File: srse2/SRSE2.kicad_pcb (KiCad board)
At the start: 2 copper layers, 82 x 72 mm, 93 parts, among them J1 s88-N, J2 CAN, P1 I2S, P10 PIC_SPARE, P11 RS485 TERM, P12 RS485, P13 CONN_01X03, P15 S88I, P17 RA5, P18 CONN_01X03, P19 CONN_01X02, P2 CONN_01X09, P20 O2P-Rst, P3 CONN_01X02, P4 CONN_01X04, P5 CONN_01X04, P6 ISO_I2C, P7 CAN_TERM, P8 CAN, P9 PIC_I2C, U1 Omega2, U10 OKI-78SR, U2 ADuM1250, U3 SN65HVD230, U4 PIC18F25K80, U5 HR911105A, U6 MAX485, U7 TPS5430DDA, U8 CD4504, U9 LM317, Y1 16MHz

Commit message: new SRSEII JLCPCB production files Version 1.8
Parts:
- U2, U6: footprint w_smd_dil:so-8 -> Package_SO:SOIC-8_3.9x4.9mm_P1.27mm
- U8: footprint w_smd_dil:so-16 -> Package_SO:SO-16_3.9x9.9mm_P1.27mm
- moved R25 5.72 mm to (122.0, 118.2)
- moved R24 3.64 mm to (126.5, 118.2), turned to 0 degrees
- moved G*** 1.65 mm to (150.8, 76.2)
- moved D3 0.56 mm to (125.2, 87.6)
- moved U10 0.50 mm to (117.7, 79.6)
- moved U9 0.41 mm to (105.7, 121.3)
- moved P13 0.35 mm to (113.2, 82.2)
- moved R9 0.29 mm to (166.4, 100.2)
- moved D2 0.26 mm to (125.2, 92.4)
- moved C1 0.14 mm to (143.6, 113.0)
- moved P4 0.11 mm to (171.4, 118.1)
- moved P20 0.11 mm to (166.0, 120.2)
- moved R104 0.08 mm to (113.1, 87.6)
- turned R103 to -90 degrees
- turned U2 to 0 degrees
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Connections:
- net Net-(D100-Pad1) renamed /PH
- net Net-(L100-Pad2) renamed /Vout
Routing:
- net +5V: track 107.5 -> 178.9 mm, vias 8 -> 10
- net VCC: track 250.1 -> 303.1 mm, vias 3 -> 4
- net /12V: track 7.40 -> 51.1 mm, vias 0 -> 1
- net +24V: track 55.3 -> 84.5 mm, vias 0 -> 2
- net GND: track 181.3 -> 200.1 mm, vias 34 -> 57
- net /Vout: track 0.00 -> 18.5 mm
- net Net-(P12-Pad4): track 10.5 -> 27.2 mm, vias 0 -> 2
- net Net-(D3-Pad1): track 0.00 -> 13.9 mm
- net Net-(R26-Pad1): track 0.00 -> 13.9 mm
- net /S88_DATA: track 5.58 -> 18.3 mm
- net /Vdd: track 10.0 -> 22.1 mm, vias 0 -> 1
- net Net-(R101-Pad2): track 0.00 -> 12.1 mm
- net Net-(P11-Pad2): track 8.05 -> 19.9 mm
- net Net-(D2-Pad1): track 0.00 -> 11.1 mm
- net Net-(C100-Pad2): track 0.00 -> 10.8 mm
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- added copper zone on F.Cu, net /PH
- added copper zone on F.Cu, net /Vout

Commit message: add new production ZIP
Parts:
- added REF**: Inlay, SRSE2:Inlay, F.Cu at (140.8, 109.8)
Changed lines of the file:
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@@
+    )
+  )
+  (footprint "SRSE2:Inlay" (layer "F.Cu")
+    (at 140.85 109.85)
+    (attr smd)
+    (fp_text reference "REF**" (at 0 -0.5 unlocked) (layer "F.SilkS")
+      (effects (font (size 1 1) (thickness 0.15)))
+    )
+    (fp_text value "Inlay" (at 0 1 unlocked) (layer "F.Fab")
+      (effects (font (size 1 1) (thickness 0.15)))
+    )
+    (fp_text user "${REFERENCE}" (at 0 2.5 unlocked) (layer "F.Fab")
+      (effects (font (size 1 1) (thickness 0.15)))
+    )
+    (fp_circle (center -33 20) (end -28 20) (layer "F.SilkS") (width 0.12) (fill none))
+    (fp_circle (center 33 -20) (end 38.211644 -20) (layer "F.SilkS") (width 0.12) (fill none))
+    (fp_circle (center 33 20) (end 38.391146 20) (layer "F.SilkS") (width 0.12) (fill none))
+    (fp_circle (center -33 -20) (end -28 -20) (layer "F.SilkS") (width 0.12) (fill none))
+    (fp_circle (center 33 20) (end 33.000001 20) (layer "F.SilkS") (width 0.12) (fill none))
+    (model "${KIPRJMOD}/inlay.wrl"
+      (offset (xyz 0 0 -4.6))
+      (scale (xyz 1 1 1))
+      (rotate (xyz 0 0 0))
     )
   )

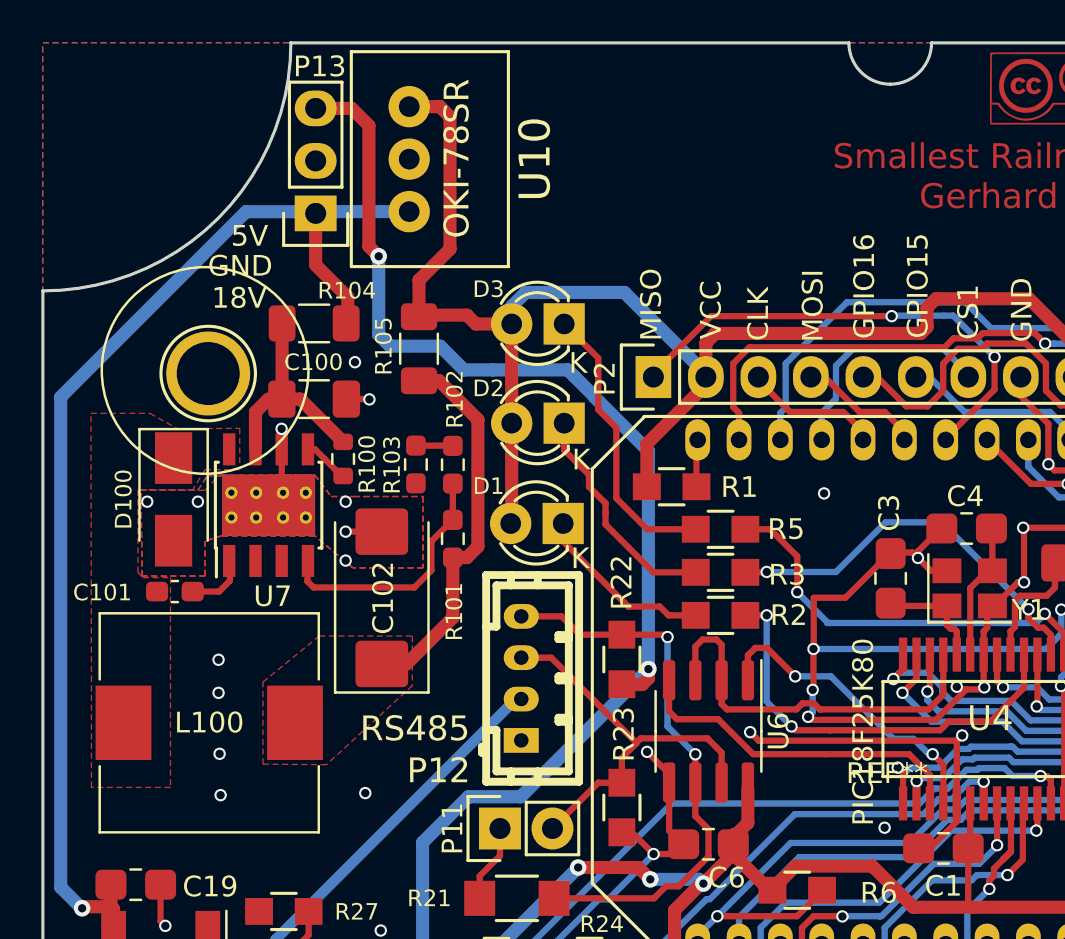
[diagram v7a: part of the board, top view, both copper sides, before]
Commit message: remove old 3V3 DCDC
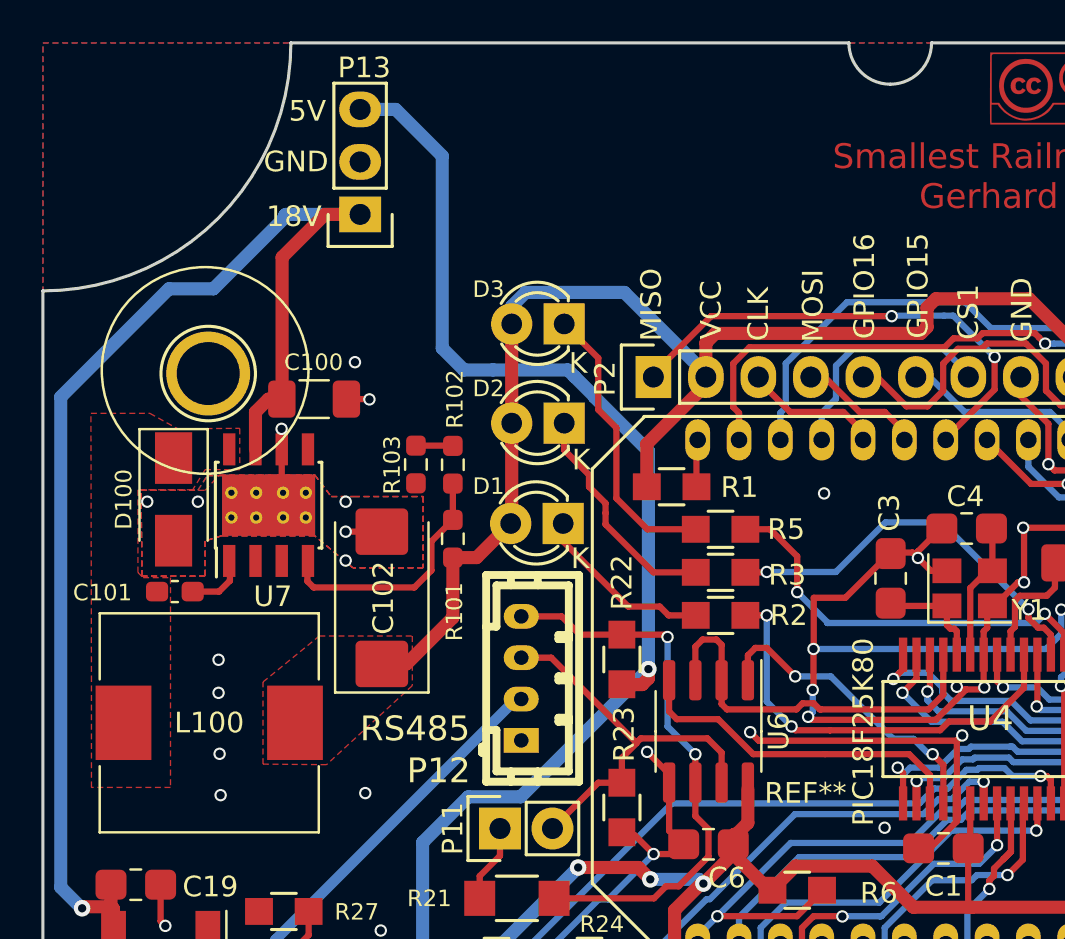
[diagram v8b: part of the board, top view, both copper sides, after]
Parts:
- removed R100: 100k, Resistor_SMD:R_0603_1608Metric
- removed R104, R105: 0, Resistor_SMD:R_1206_3216Metric_Pad1.30x1.75mm_HandSolder
- removed U10: OKI-78SR, common-ICs:OKI-78SR
- moved P13 2.15 mm to (115.3, 82.3)
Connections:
- C100 pad 2: Net-(C100-Pad2) -> +24V
- C102 pad 1: /Vout -> VCC
- L100 pad 2: /Vout -> VCC
- R101 pad 1: /Vout -> VCC
- U7 pad 5: Net-(R100-Pad2) -> unconnected-(U7-Pad5)
- U7 pad 7: Net-(C100-Pad2) -> +24V
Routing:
- net /Vout: track 18.5 -> 0.00 mm
- net Net-(C100-Pad2): track 10.8 -> 0.00 mm
- net VCC: track 303.1 -> 296.6 mm
- net +24V: track 84.5 -> 90.7 mm
- net +5V: track 178.9 -> 176.6 mm, vias 10 -> 9
- net Net-(R100-Pad2): track 2.24 -> 0.00 mm
- added copper zone on F.Cu, net VCC
- removed copper zone on F.Cu, net /Vout
